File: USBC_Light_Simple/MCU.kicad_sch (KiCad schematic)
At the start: 1 part, among them U5 STM32C011F6Px

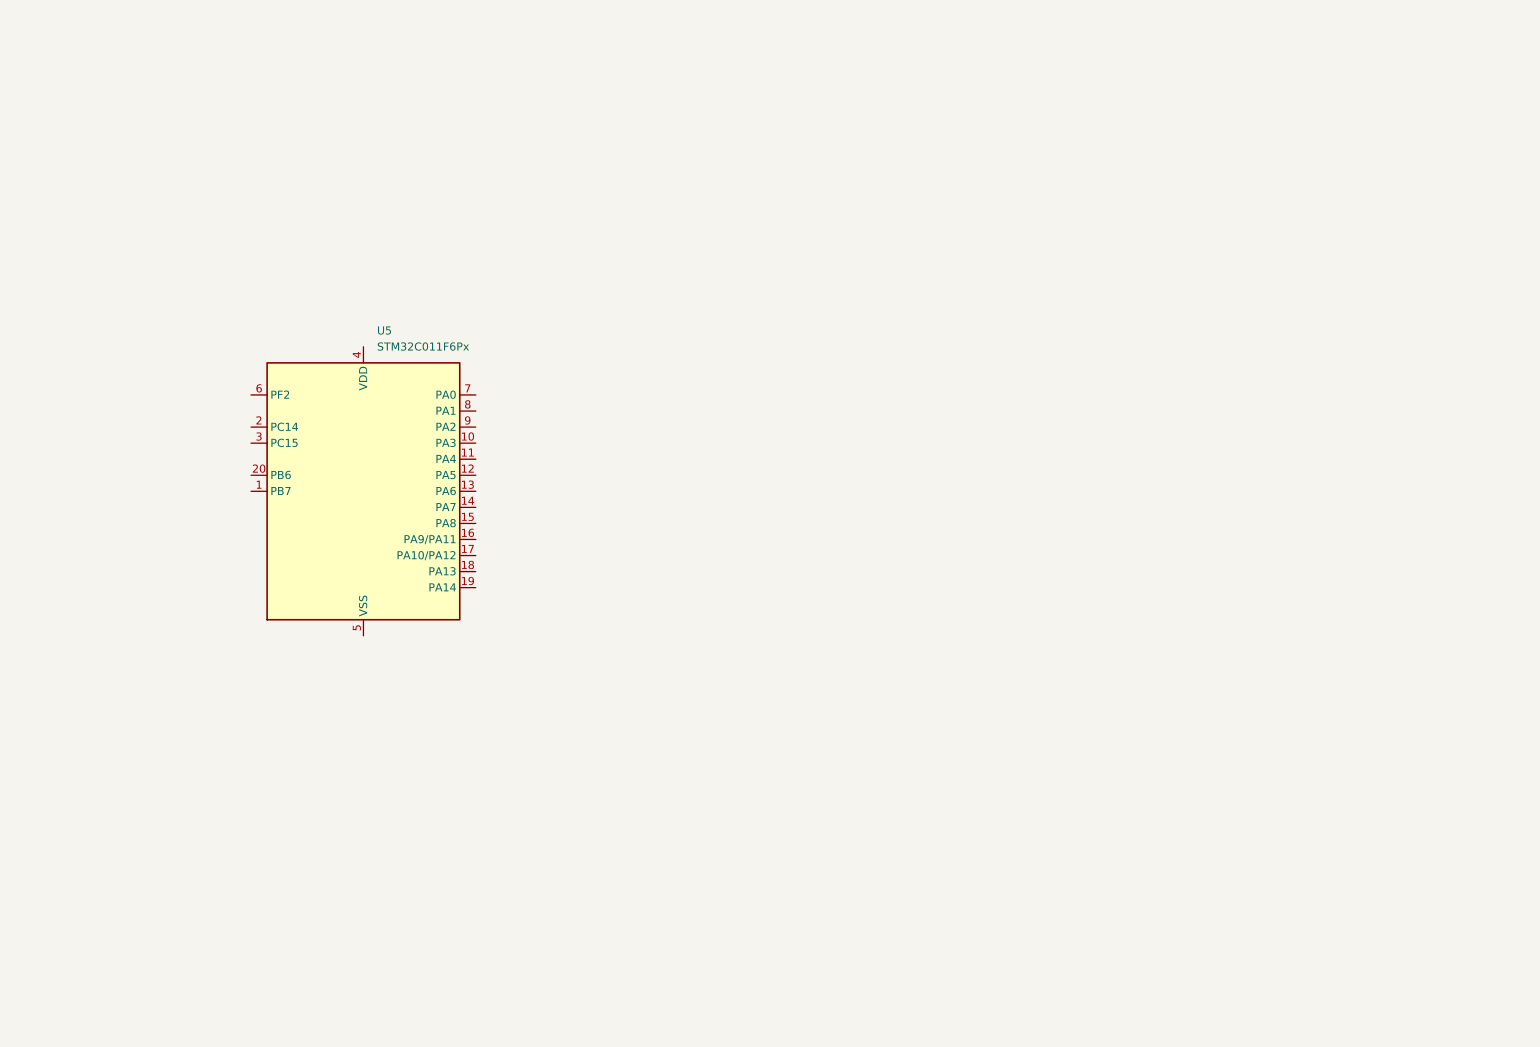
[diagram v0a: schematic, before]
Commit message: Fleshed out most of schematic. Now need to add component vals.
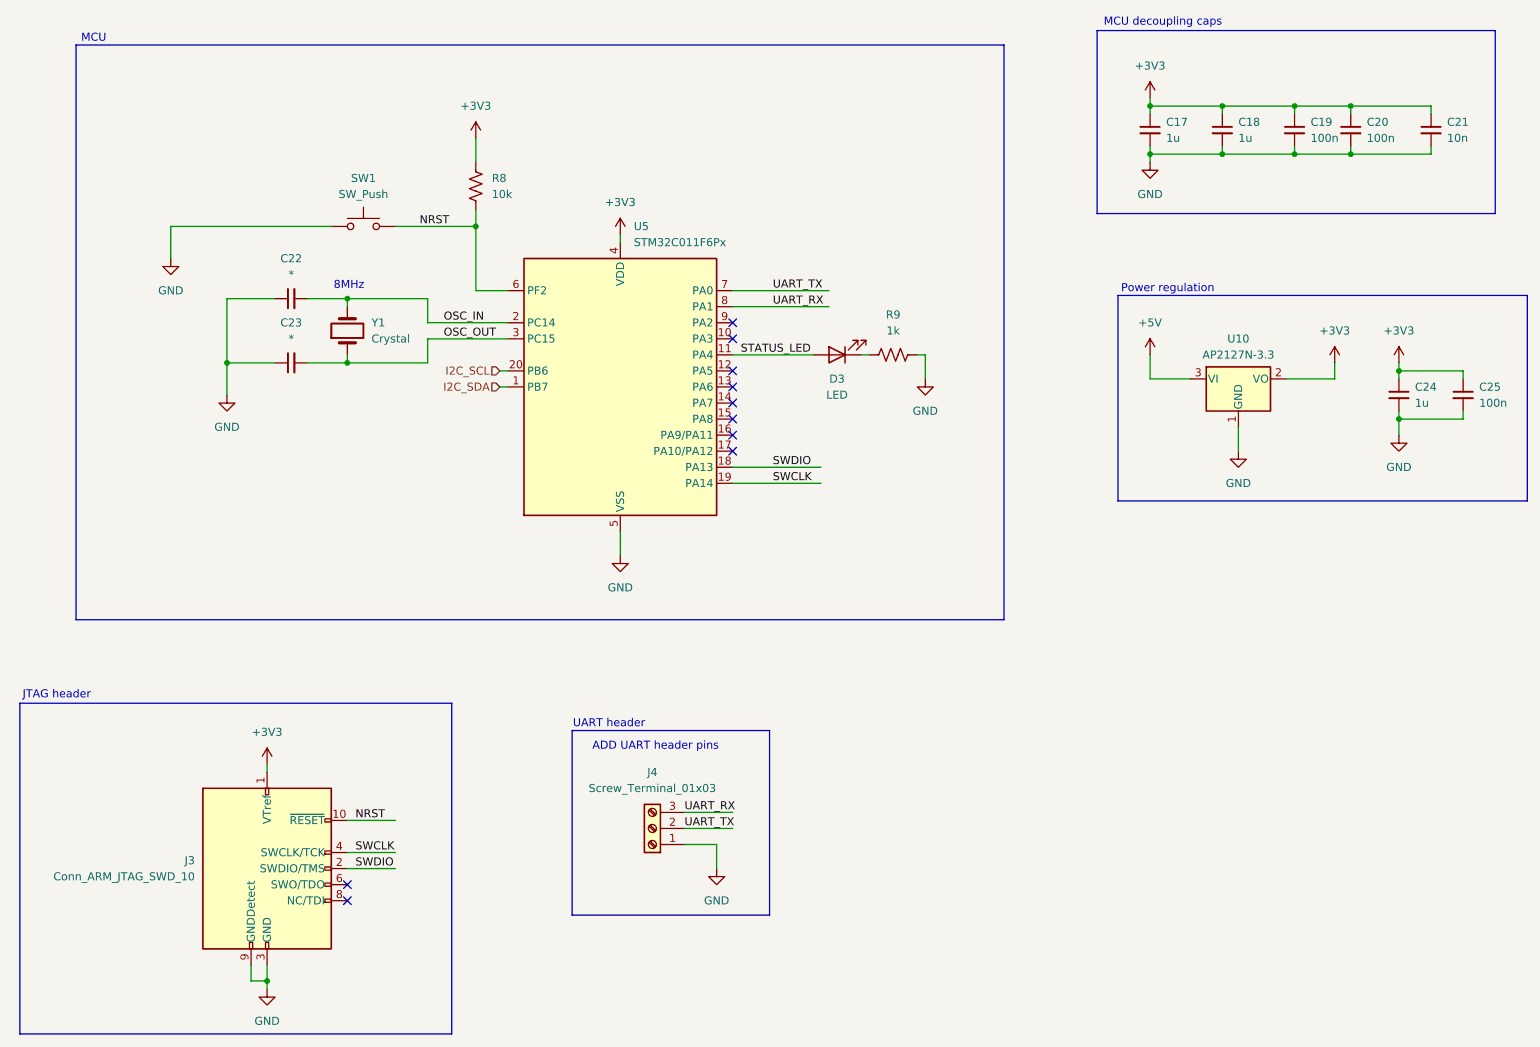
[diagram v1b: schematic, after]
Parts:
- added C17, C18, C24: 1u, symbol Device:C_Small
- added C19, C20, C25: 100n, symbol Device:C_Small
- added C21: 10n, symbol Device:C_Small
- added C22, C23: *, symbol Device:C_Small
- added D3: LED, symbol Device:LED
- added J3: Conn_ARM_JTAG_SWD_10, symbol Connector:Conn_ARM_JTAG_SWD_10
- added J4: Screw_Terminal_01x03, symbol Connector:Screw_Terminal_01x03
- added R8: 10k, symbol Device:R_US
- added R9: 1k, symbol Device:R_US
- added SW1: SW_Push, symbol Switch:SW_Push
- added U10: AP2127N-3.3, Package_TO_SOT_SMD:SOT-23, symbol Regulator_Linear:AP2127N-3.3
- added Y1: Crystal, symbol Device:Crystal
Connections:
- net I2C_SDA: now reaches U5.1 (PB7)
- net STATUS_LED: now reaches U5.11 (PA4)
- net STATUS_LED: now also D3.2 (A)
- net SWDIO: now reaches U5.18 (PA13)
- net SWDIO: now also J3.2 (SWDIO/TMS)
- net SWCLK: now reaches U5.19 (PA14)
- net SWCLK: now also J3.4 (SWCLK/TCK)
- net OSC_IN: now reaches U5.2 (PC14)
- net OSC_IN: now also C22.2, Y1.2
- net I2C_SCL: now reaches U5.20 (PB6)
- net OSC_OUT: now reaches U5.3 (PC15)
- net OSC_OUT: now also C23.2, Y1.1
- net +3V3: now reaches U5.4 (VDD)
- net +3V3: now also C17.1, C18.1, C19.1, C20.1, C21.1, C24.1, C25.1, J3.1 (VTref), R8.1, U10.2 (VO)
- net GND: now reaches U5.5 (VSS)
- net GND: now also C17.2, C18.2, C19.2, C20.2, C21.2, C22.1, C23.1, C24.2, C25.2, J3.3 (GND), J3.5 (GND), J3.9 (GNDDetect), J4.1 (Pin_1), R9.1, SW1.1, U10.1 (GND)
- net NRST: now reaches U5.6 (PF2)
- net NRST: now also J3.10 (~{RESET}), R8.2, SW1.2
- net UART_TX: now reaches U5.7 (PA0)
- net UART_TX: now also J4.2 (Pin_2)
- net UART_RX: now reaches U5.8 (PA1)
- net UART_RX: now also J4.3 (Pin_3)
- new net: D3.1 (K), R9.2
- new net +5V: U10.3 (VI)
- no-connect marks 0 -> 10
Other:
- note added: "8MHz"
- note added: "ADD UART header pins"
- note added: "JTAG header"
- note added: "MCU"
- note added: "MCU decoupling caps"
- note added: "Power regulation"
- note added: "UART header"
- moved on the sheet: U5

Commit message: Preliminary component placement on board.
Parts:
- C17, C18, C19, C20, C21, C22, C23, C24, C25: footprint (none) -> Capacitor_SMD:C_0603_1608Metric_Pad1.08x0.95mm_HandSolder
- D3: footprint (none) -> LED_SMD:LED_0603_1608Metric_Pad1.05x0.95mm_HandSolder
- J4: footprint (none) -> Connector_PinHeader_1.00mm:PinHeader_1x03_P1.00mm_Vertical
- R8, R9: footprint (none) -> Resistor_SMD:R_0603_1608Metric_Pad0.98x0.95mm_HandSolder
- SW1: footprint (none) -> Button_Switch_THT:SW_PUSH_6mm
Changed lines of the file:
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@@
 			)
 		)
-		(property "Footprint" ""
+		(property "Footprint" "Capacitor_SMD:C_0603_1608Metric_Pad1.08x0.95mm_HandSolder"
 			(at 229.87 36.83 0)
 			(effects
@@
 			)
 		)
-		(property "Footprint" ""
+		(property "Footprint" "Resistor_SMD:R_0603_1608Metric_Pad0.98x0.95mm_HandSolder"
 			(at 112.776 45.974 90)
 			(effects
@@
 			)
 		)
-		(property "Footprint" ""
+		(property "Footprint" "LED_SMD:LED_0603_1608Metric_Pad1.05x0.95mm_HandSolder"
 			(at 168.91 72.39 0)
 			(effects
@@
 			)
 		)
-		(property "Footprint" ""
+		(property "Footprint" "Capacitor_SMD:C_0603_1608Metric_Pad1.08x0.95mm_HandSolder"
 			(at 218.44 36.83 0)
 			(effects
@@
 			)
 		)
-		(property "Footprint" ""
+		(property "Footprint" "Capacitor_SMD:C_0603_1608Metric_Pad1.08x0.95mm_HandSolder"
 			(at 82.55 63.5 0)
 			(effects
@@
 			)
 		)
-		(property "Footprint" ""
+		(property "Footprint" "Button_Switch_THT:SW_PUSH_6mm"
 			(at 93.98 46.99 0)
 			(effects
@@
 			)
 		)
-		(property "Footprint" ""
+		(property "Footprint" "Capacitor_SMD:C_0603_1608Metric_Pad1.08x0.95mm_HandSolder"
 			(at 262.89 36.83 0)
 			(effects
@@
 			)
 		)
-		(property "Footprint" ""
+		(property "Footprint" "Capacitor_SMD:C_0603_1608Metric_Pad1.08x0.95mm_HandSolder"
 			(at 267.97 78.74 0)
 			(effects
@@
 			)
 		)
-		(property "Footprint" ""
+		(property "Footprint" "Capacitor_SMD:C_0603_1608Metric_Pad1.08x0.95mm_HandSolder"
 			(at 82.55 73.66 0)
 			(effects
@@
 			)
 		)
-		(property "Footprint" ""
+		(property "Footprint" "Resistor_SMD:R_0603_1608Metric_Pad0.98x0.95mm_HandSolder"
 			(at 177.546 73.406 90)
 			(effects
@@
 			)
 		)
-		(property "Footprint" ""
+		(property "Footprint" "Capacitor_SMD:C_0603_1608Metric_Pad1.08x0.95mm_HandSolder"
 			(at 250.19 36.83 0)
 			(effects
@@
 			)
 		)
-		(property "Footprint" ""
+		(property "Footprint" "Connector_PinHeader_1.00mm:PinHeader_1x03_P1.00mm_Vertical"
 			(at 139.7 147.32 0)
 			(effects
@@
 			)
 		)
-		(property "Footprint" ""
+		(property "Footprint" "Capacitor_SMD:C_0603_1608Metric_Pad1.08x0.95mm_HandSolder"
 			(at 241.3 36.83 0)
 			(effects
@@
 			)
 		)
-		(property "Footprint" ""
+		(property "Footprint" "Capacitor_SMD:C_0603_1608Metric_Pad1.08x0.95mm_HandSolder"
 			(at 257.81 78.74 0)
 			(effects
